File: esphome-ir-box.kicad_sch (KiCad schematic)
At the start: 16 parts, among them J1 Conn_01x15_Female, J2 Conn_01x15_Female, J3 Conn_01x15_Male, J4 Conn_01x15_Male, Q1 2N7000, Q2 2N7000, Q3 2N7000, U1 VS1838B

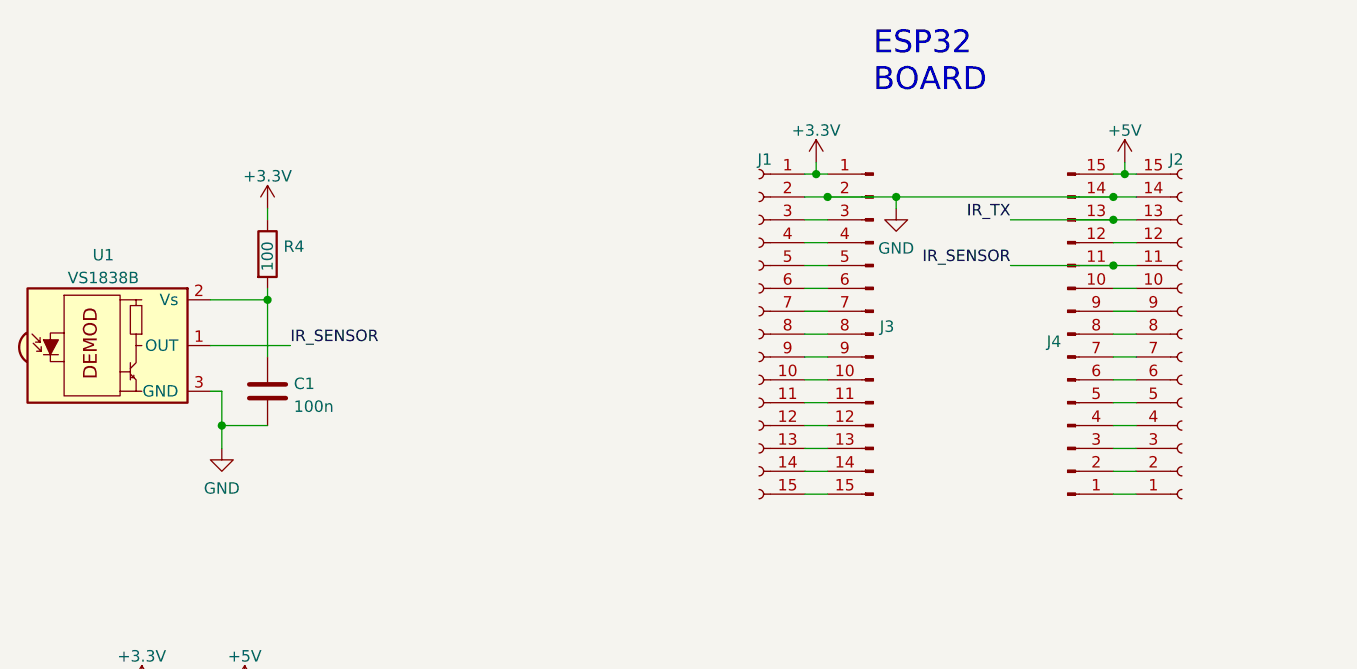
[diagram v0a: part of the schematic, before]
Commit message: Fix VS1813B pinout, KiCad 7 tweaks
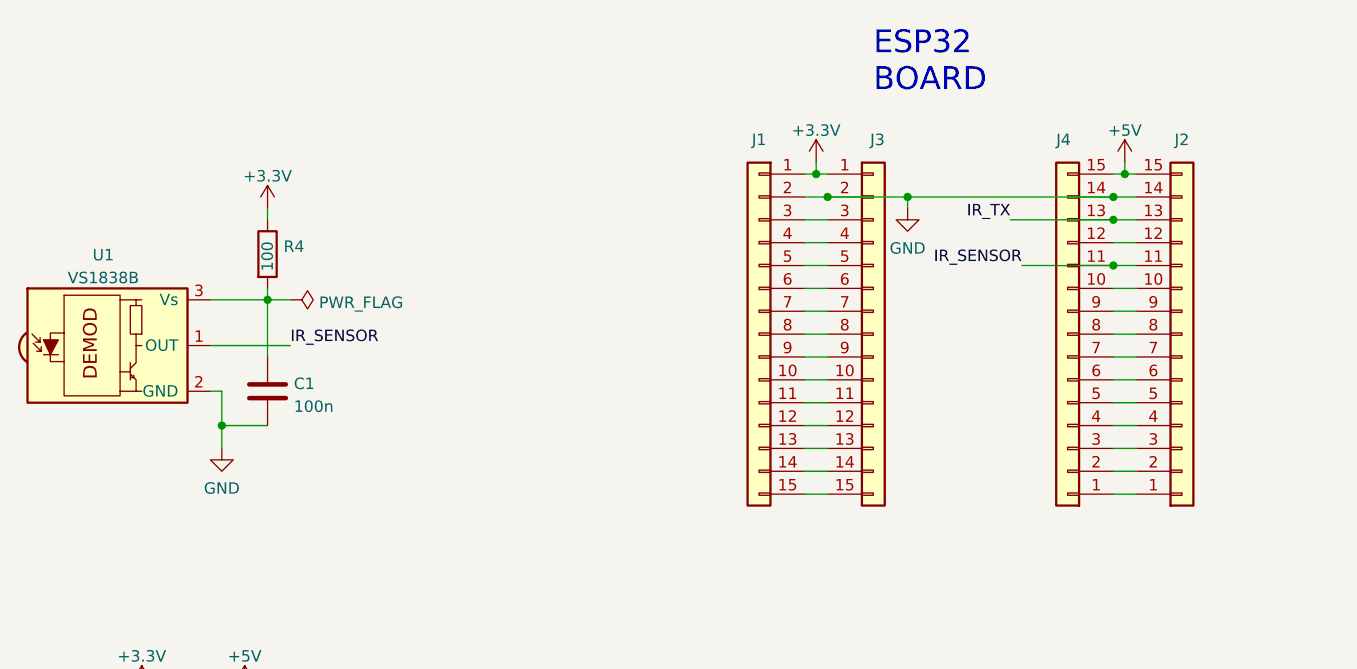
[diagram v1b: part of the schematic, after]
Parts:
- J1, J2: symbol Connector:Conn_01x15_Female -> Connector_Generic:Conn_01x15
- J3, J4: symbol Connector:Conn_01x15_Male -> Connector_Generic:Conn_01x15
- U1: symbol Interface_Optical:TSOP325xx -> vs1838b:VS1838B
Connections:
- net GND: now also U1.2 (GND); no longer U1.3 (GND)
- net at C1.1, R4.2: now also U1.3 (Vs); no longer U1.2 (Vs)

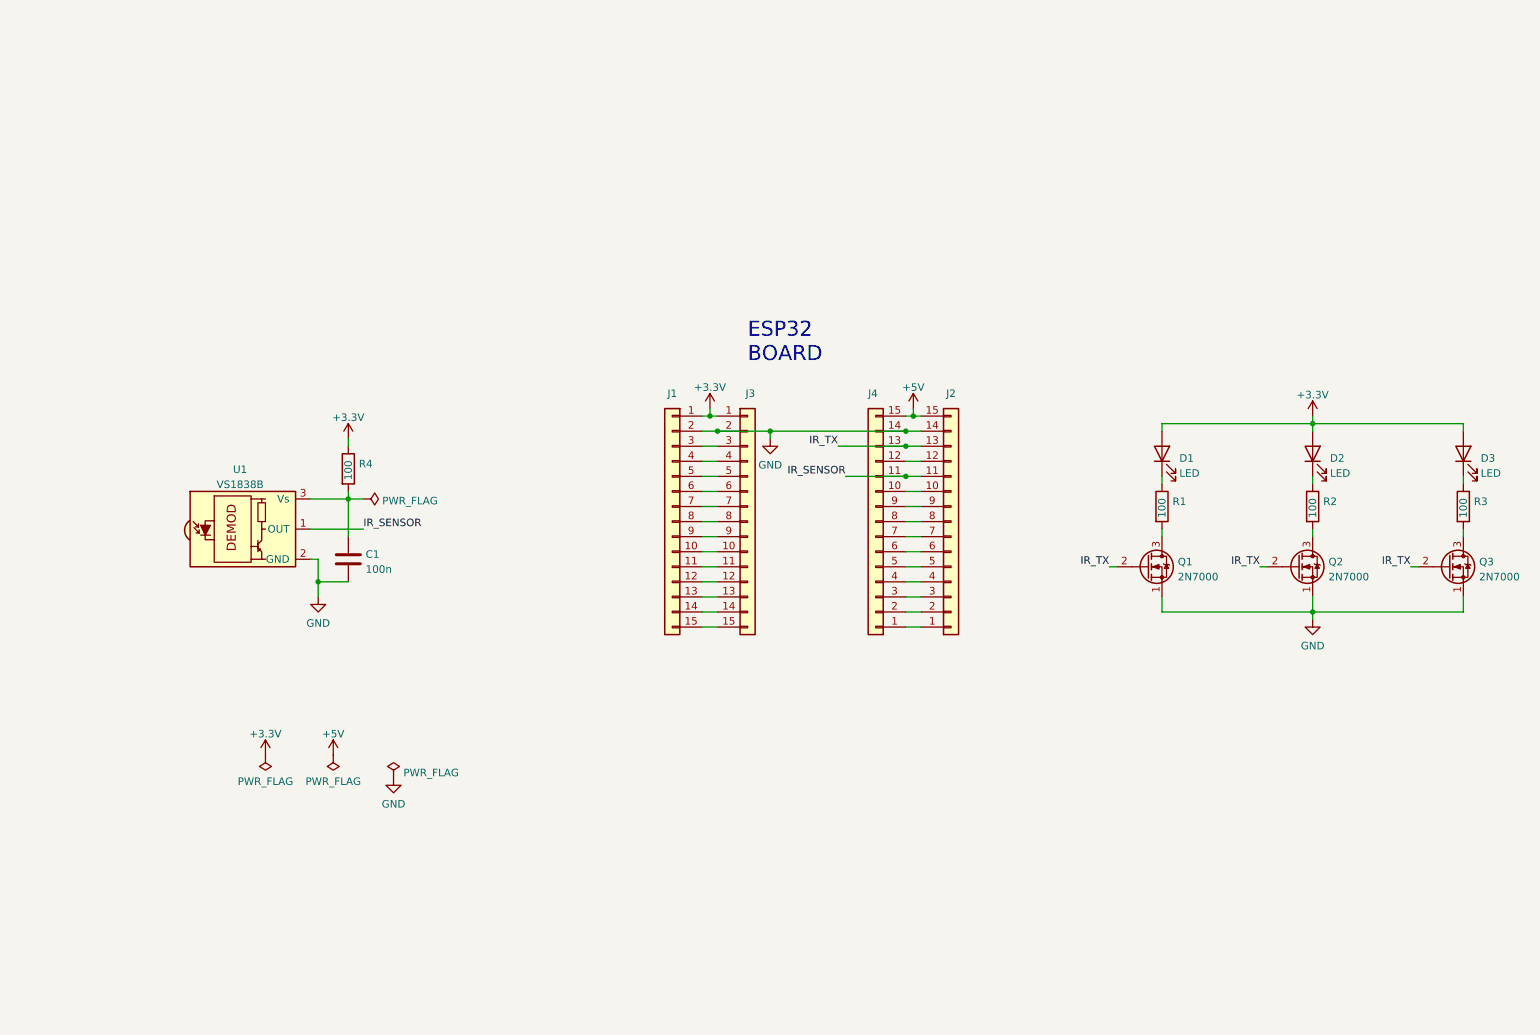
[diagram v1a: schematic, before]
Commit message: Revise board, focussing on building into devices
New board layout has very few onboard components, and focuses on wiring
an IR LED into an existing device (next to its sensor), while leeching
power of the host device and piggybacking off its IR sensor.

There are jumpers for selecting input voltage (5V or 3.3V) which
determines where power gets routed to on the esp32 dev board, as well as
a bypassable voltage divider for the IR input. So if the host device
runs the IR sensor at 5V, it is selectable on this board, so it's
lowered to ~3.3V before going into the ESP32.

The IR Led connection to resistor/esp32 is also optional with a pair of
jumpers, so the connector can be used for other purposes if needed.

Lastly, there's a "protoboard" area for a small bit of custom circuitry
/ connectors, along with several power connection points.
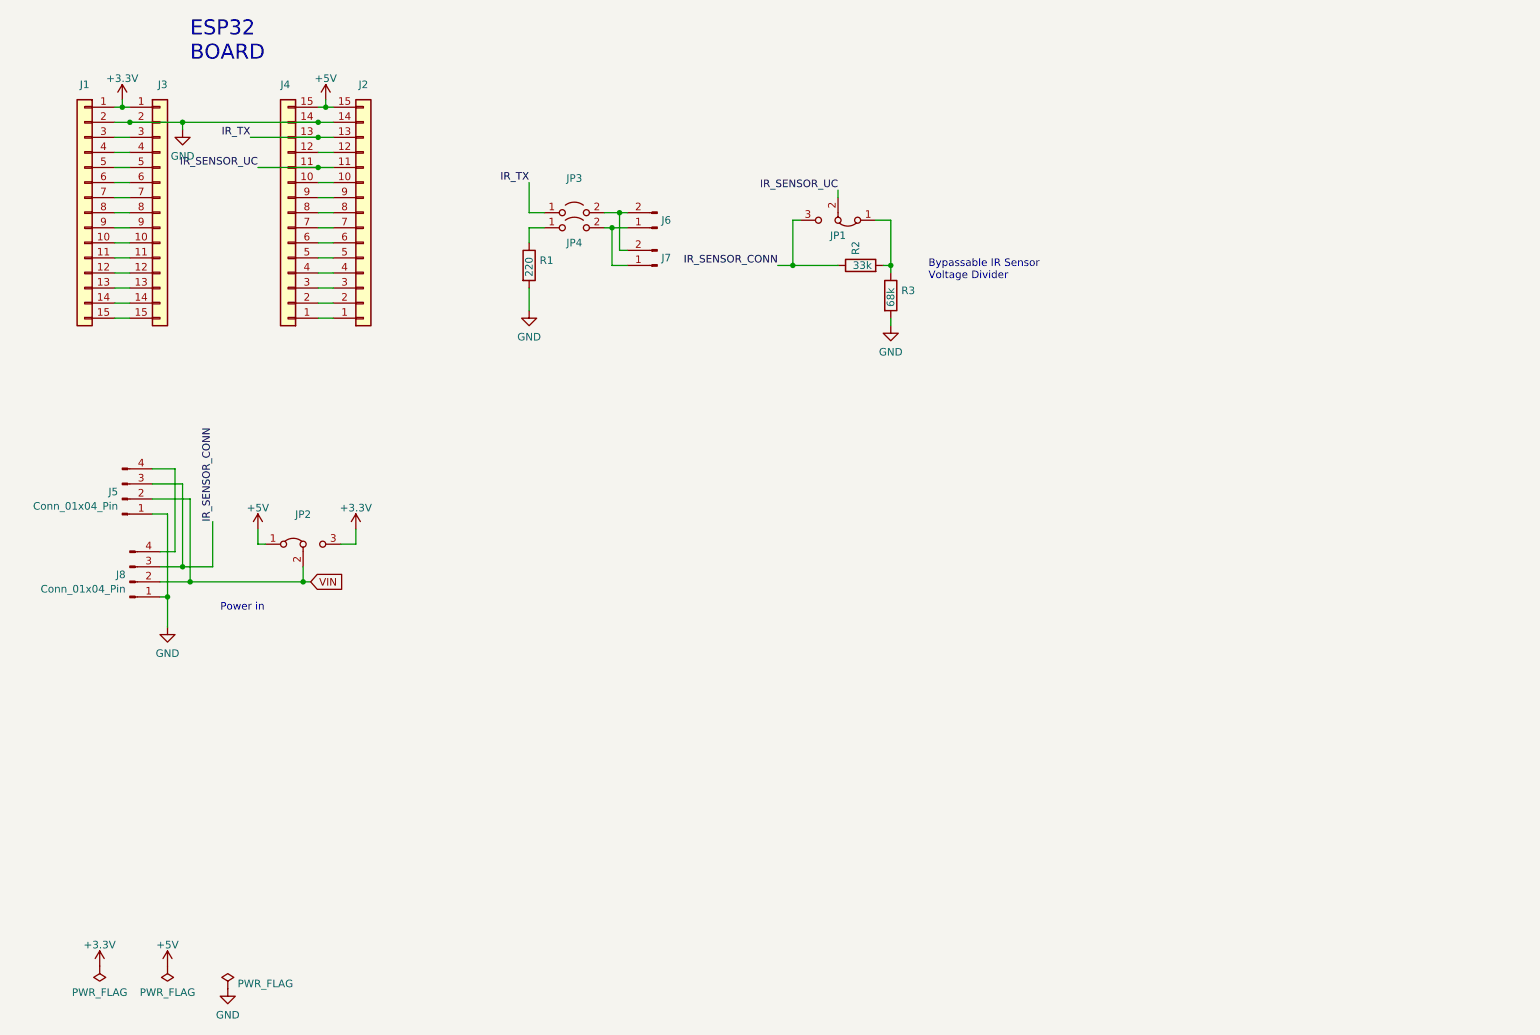
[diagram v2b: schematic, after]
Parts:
- removed C1: 100n, Capacitor_THT:C_Disc_D4.7mm_W2.5mm_P5.00mm, symbol Device:C
- removed D1, D2, D3: LED, LED_THT:LED_D5.0mm_Clear, symbol Device:LED
- removed Q1, Q2, Q3: 2N7000, Package_TO_SOT_THT:TO-92_Inline, symbol Transistor_FET:2N7000
- removed R4: 100, Resistor_THT:R_Axial_DIN0207_L6.3mm_D2.5mm_P7.62mm_Horizontal, symbol Device:R
- removed U1: VS1838B, OptoDevice:Vishay_MOLD-3Pin, symbol vs1838b:VS1838B
- added J5: Conn_01x04_Pin, Connector_PinHeader_2.54mm:PinHeader_1x04_P2.54mm_Vertical, symbol Connector:Conn_01x04_Pin
- added J6: Conn_01x02_Pin, Connector_JST:JST_PH_S2B-PH-K_1x02_P2.00mm_Horizontal, symbol Connector:Conn_01x02_Pin
- added J7: Conn_01x02_Pin, Connector_PinHeader_2.54mm:PinHeader_1x02_P2.54mm_Vertical, symbol Connector:Conn_01x02_Pin
- added J8: Conn_01x04_Pin, Connector_JST:JST_PH_S4B-PH-K_1x04_P2.00mm_Horizontal, symbol Connector:Conn_01x04_Pin
- added JP1, JP2: Jumper_3_Bridged12, Jumper:SolderJumper-3_P2.0mm_Open_TrianglePad1.0x1.5mm, symbol Jumper:Jumper_3_Bridged12
- added JP3, JP4: Jumper_2_Open, Jumper:SolderJumper-2_P1.3mm_Open_TrianglePad1.0x1.5mm, symbol Jumper:Jumper_2_Open
- R1: value 100 -> 220; footprint Resistor_THT:R_Axial_DIN0207_L6.3mm_D2.5mm_P7.62mm_Horizontal -> Resistor_SMD:R_0603_1608Metric; LCSC (none) -> C22962
- R2: value 100 -> 33k; footprint Resistor_THT:R_Axial_DIN0207_L6.3mm_D2.5mm_P7.62mm_Horizontal -> Resistor_SMD:R_0603_1608Metric; LCSC (none) -> C4216
- R3: value 100 -> 68k; footprint Resistor_THT:R_Axial_DIN0207_L6.3mm_D2.5mm_P7.62mm_Horizontal -> Resistor_SMD:R_0603_1608Metric; LCSC (none) -> C23231
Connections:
- net +3.3V: now also JP2.3 (B)
- net +5V: now also JP2.1 (A)
- net GND: now also R1.2, R3.2, J5.1 (Pin_1), J8.1 (Pin_1)
- net IR_TX: now also JP3.1 (A)
- net at R3.1: now also R2.2, JP1.1 (A)
- net IR_SENSOR_CONN: now reaches R2.1
- net IR_SENSOR_CONN: now also J5.3 (Pin_3), J8.3 (Pin_3), JP1.3 (B)
- net at R1.1: now also JP4.1 (A)
- net IR_SENSOR renamed IR_SENSOR_UC
- net IR_SENSOR_UC: now also JP1.2 (C)
- new net: J6.2 (Pin_2), J7.2 (Pin_2), JP3.2 (B)
- new net: J6.1 (Pin_1), J7.1 (Pin_1), JP4.2 (B)
- new net: J5.4 (Pin_4), J8.4 (Pin_4)
- new net VIN: J5.2 (Pin_2), J8.2 (Pin_2), JP2.2 (C)
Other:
- note added: "Bypassable IR Sensor Voltage Divider"
- note added: "Power in"
- company: (none) -> MichD
- moved on the sheet: J1, J2, J3, J4, R1
